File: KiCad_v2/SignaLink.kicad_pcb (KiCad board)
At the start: 2 copper layers, 63.2 x 42 mm, 91 parts, among them U1 MT3608, U1 TPS55340RTER, U2 ESP32-C3_SUPERMINI_TH, U3 DM-OLED096-636, U4 MPU-6050, U5 BNO085, U6 MCP73871, U7 LTC4415IMSE_PBF, U8 TPS54331

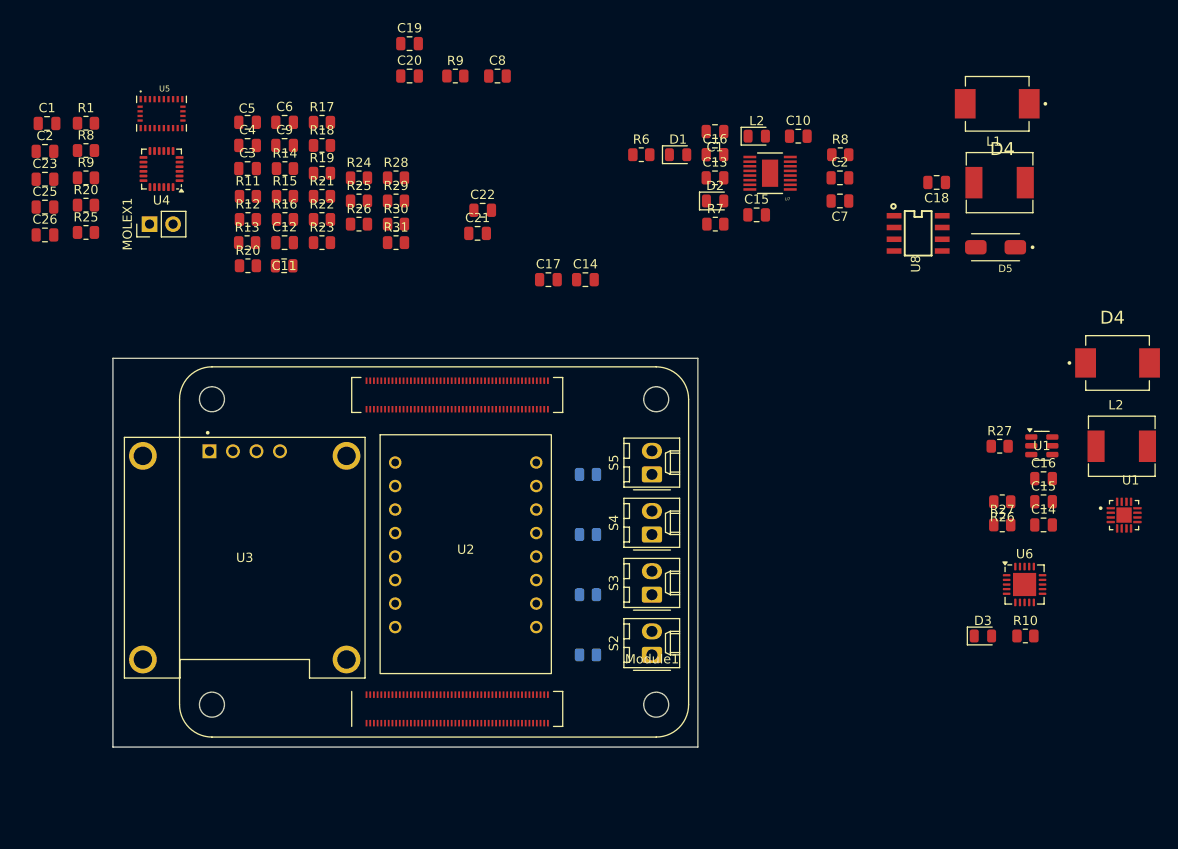
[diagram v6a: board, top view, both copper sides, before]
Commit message: Resistencias calculadas, esquematico terminado
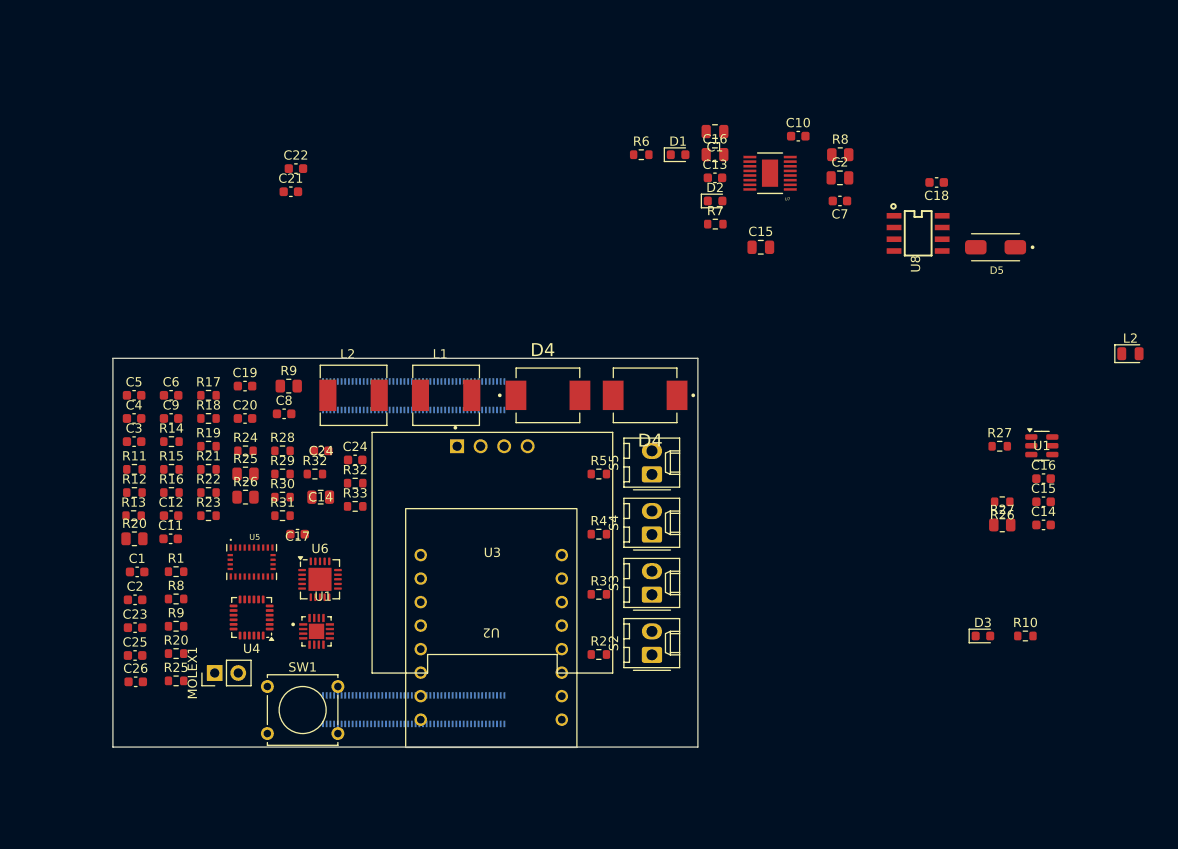
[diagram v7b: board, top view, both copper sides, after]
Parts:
- added C24: 100nf, Capacitor_SMD:C_0603_1608Metric, F.Cu at (56.2, 60.0)
- added C24: 100nF, Capacitor_SMD:C_0603_1608Metric, F.Cu at (52.5, 59.0)
- added R32: 10k, Resistor_SMD:R_0603_1608Metric, F.Cu at (51.8, 61.5)
- added R32: 10k, Resistor_SMD:R_0603_1608Metric, F.Cu at (56.2, 62.5)
- added R33: 10k, Resistor_SMD:R_0603_1608Metric, F.Cu at (56.2, 65.0)
- added SW1: SW_Wake, Button_Switch_THT:SW_Tactile_Straight_KSA0Axx1LFTR, F.Cu at (46.7, 84.5)
- C1, C10, C11, C12, C13, C14, C15, C16, C17, C18, C19, C2, C20, C21, C22, C23, C25, C26, C3, C4, C5, C6, C7, C8, C9: footprint Capacitor_SMD:C_0805_2012Metric -> Capacitor_SMD:C_0603_1608Metric
- D1, D2, D3: footprint LED_SMD:LED_0805_2012Metric -> LED_SMD:LED_0603_1608Metric
- Module1: moved to B.Cu
- R1, R10, R11, R12, R13, R14, R15, R16, R17, R18, R19, R20, R21, R22, R23, R24, R25, R26, R27, R28, R29, R30, R31, R6, R7, R8, R9: footprint Resistor_SMD:R_0805_2012Metric -> Resistor_SMD:R_0603_1608Metric
- R2, R3, R4, R5: footprint Resistor_SMD:R_0805_2012Metric -> Resistor_SMD:R_0603_1608Metric; moved to F.Cu
- moved U1 88.1 mm to (52.0, 78.5)
- moved L2 83.2 mm to (56.0, 53.0)
- moved U6 76.1 mm to (52.4, 72.9)
- moved L1 64.1 mm to (66.0, 53.0)
- moved D4 61.6 mm to (77.0, 53.0)
- moved C1 49.4 mm to (32.6, 72.1)
- moved C2 49.4 mm to (32.4, 75.1)
- moved C25 49.4 mm to (32.4, 81.1)
- moved R20 49.4 mm to (36.8, 80.9)
- moved R8 49.4 mm to (36.8, 75.0)
- moved R9 49.4 mm to (36.8, 78.0)
- moved U4 49.4 mm to (45.0, 77.0)
- moved U5 49.4 mm to (45.0, 71.0)
- moved C23 49.4 mm to (32.4, 78.1)
- moved R1 49.4 mm to (36.8, 72.0)
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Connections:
- Module1 pad 58: unconnected-(Module1A-GPIO2-Pad58) -> Net-(Module1A-GPIO2)
- Module1 pad 99: unconnected-(Module1A-Global_EN-Pad99) -> Net-(Module1A-Global_EN)
- R6 pad 1: /power_supply/PGEN -> GND
- U6 pad 6: /power_supply/PGEN -> GND

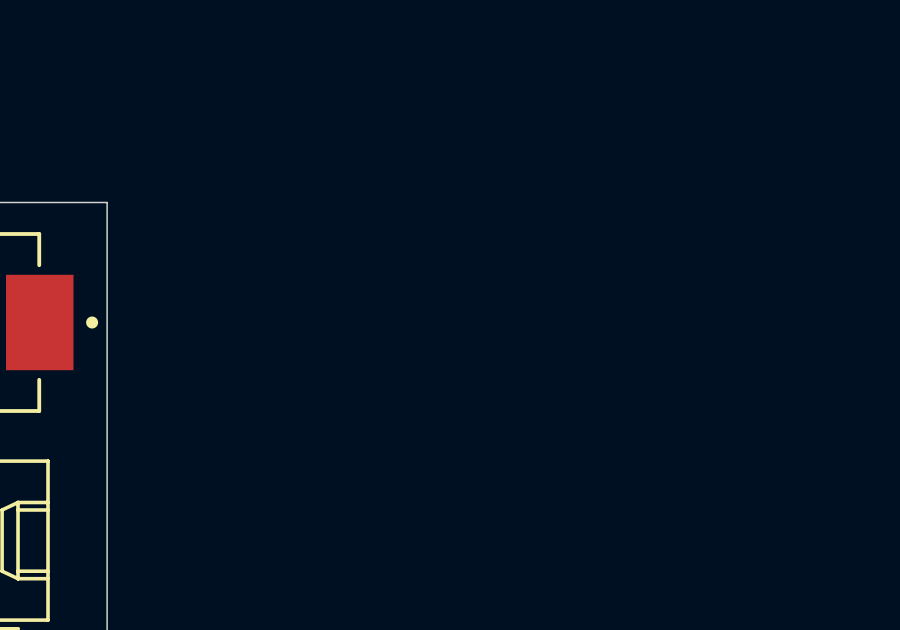
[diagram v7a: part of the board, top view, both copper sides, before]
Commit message: agrego LT8582
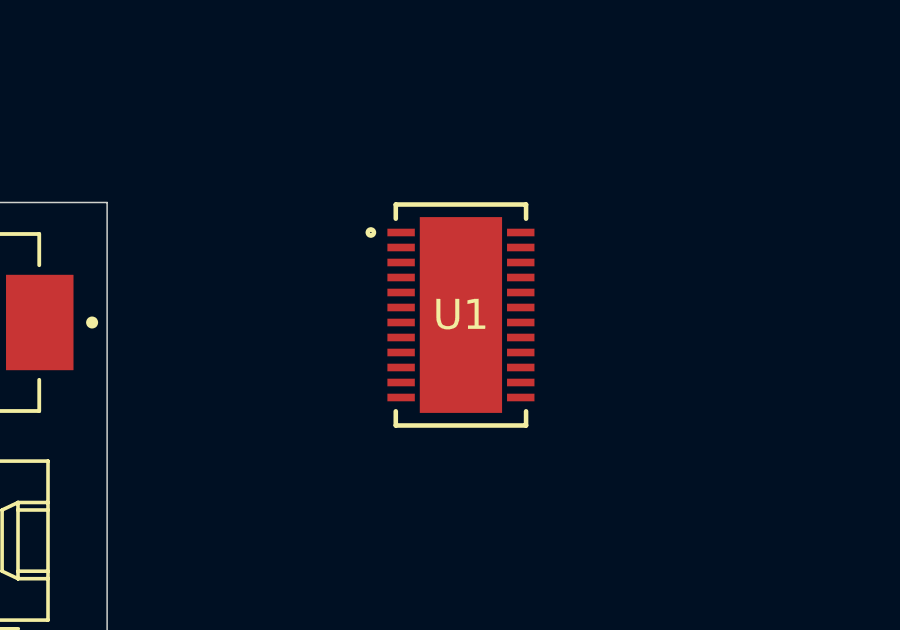
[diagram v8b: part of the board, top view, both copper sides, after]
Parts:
- added U1: LT8582EDKD-PBF, Custom_Footprints:DKD_ADI-M, F.Cu at (105.0, 52.7)
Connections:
- R6 pad 1: GND -> /power_supply/PGEN
- U6 pad 6: GND -> /power_supply/PGEN
